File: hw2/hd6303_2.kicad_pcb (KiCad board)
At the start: 2 copper layers, 29 parts, among them J1 Conn_02x20_Odd_Even, J2 Conn_02x06_Odd_Even, J3 Screw_Terminal_01x02, SW1 SW_Push, U2 MAX708, U3 27C512, U4 HD6303RP, U5 HM62256BLP-7, U6 GAL16V8, Y1 4.9152M

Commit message: still making progress...
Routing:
- net /-WMEM: track 0.00 -> 74.9 mm, vias 0 -> 2
- net /-IOEN3: track 0.00 -> 71.3 mm, vias 0 -> 3
- net /-IOEN1: track 0.00 -> 71.0 mm, vias 0 -> 3
- net /-IOEN0: track 0.00 -> 70.9 mm, vias 0 -> 3
- net /-IOEN2: track 0.00 -> 69.7 mm, vias 0 -> 2
- net /A0: track 67.1 -> 135.7 mm, vias 2 -> 4
- net /A1: track 61.9 -> 125.8 mm, vias 2 -> 4
- net /A2: track 57.1 -> 115.8 mm, vias 0 -> 2
- net /A3: track 59.3 -> 111.6 mm, vias 2 -> 4
- net /A4: track 64.4 -> 112.0 mm, vias 2 -> 4
- net /A5: track 69.3 -> 112.8 mm, vias 2 -> 4
- net /A6: track 74.1 -> 113.0 mm, vias 2 -> 4
- net /A7: track 78.8 -> 110.9 mm, vias 1 -> 2
- net /P22: track 0.00 -> 23.2 mm, vias 0 -> 1
- net /P21: track 0.00 -> 22.5 mm, vias 0 -> 1
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
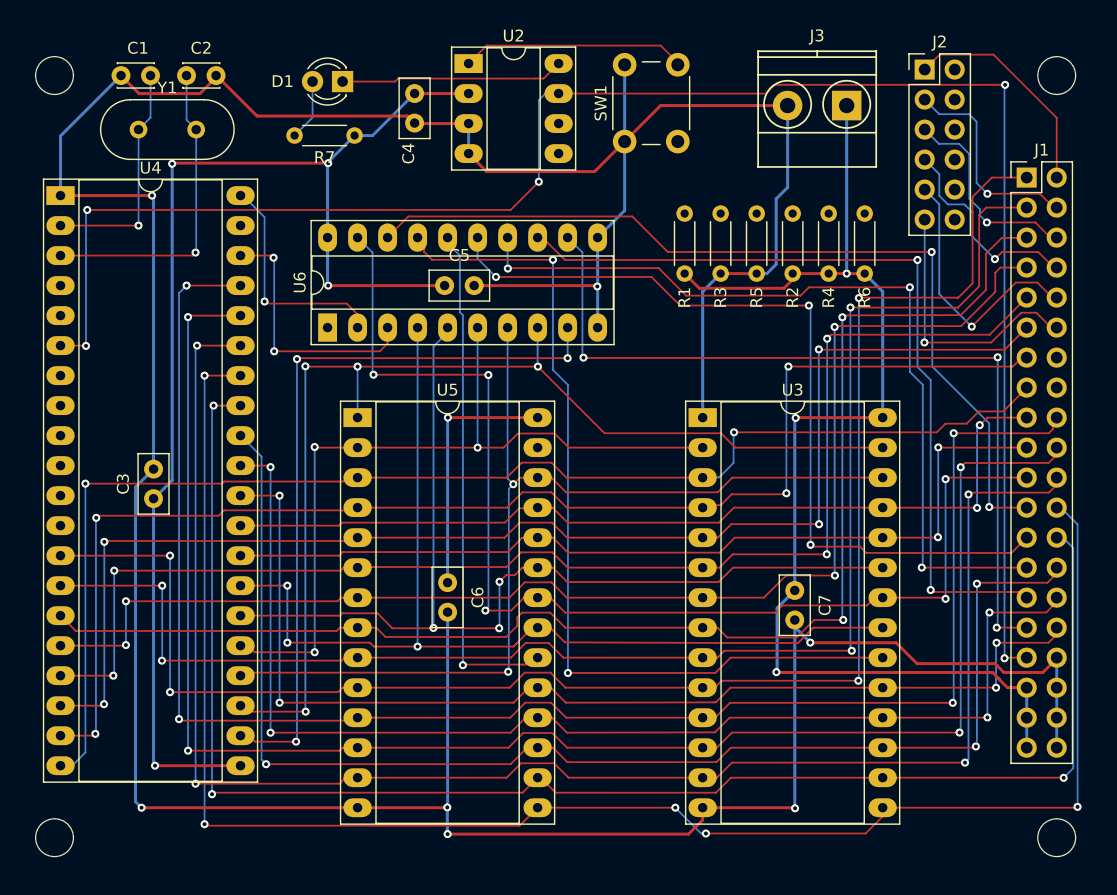
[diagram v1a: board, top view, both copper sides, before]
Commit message: all traces on expansion header routed
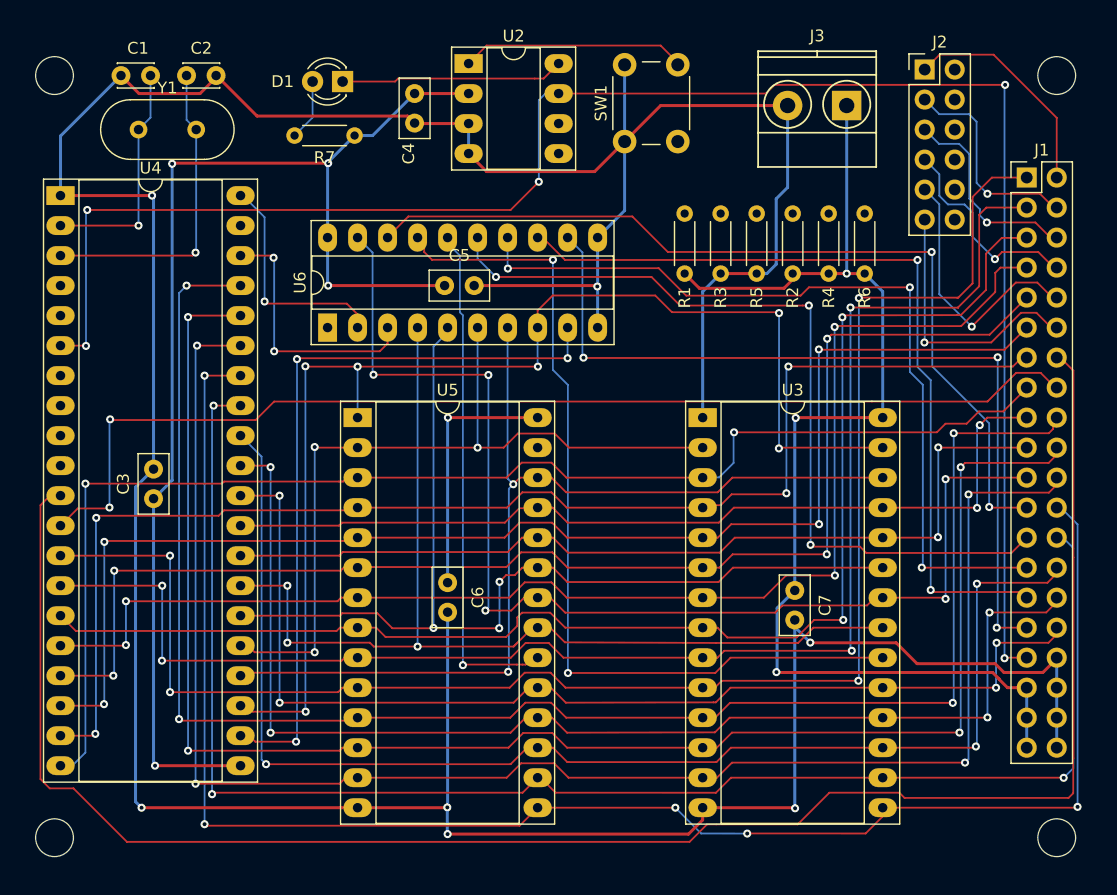
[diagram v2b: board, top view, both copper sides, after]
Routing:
- net /P23: track 0.00 -> 154.6 mm
- net /P24: track 0.00 -> 94.6 mm, vias 0 -> 2
- net /A14: track 94.4 -> 105.7 mm, vias 4 -> 6
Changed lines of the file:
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@@
   (general
     (links 155)
-    (no_connects 19)
+    (no_connects 17)
     (area 66.144857 85.645 178.203143 159.819)
     (thickness 1.6)
     (drawings 0)
-    (tracks 919)
+    (tracks 969)
     (zones 0)
     (modules 29)
@@
   (segment (start 83.058 146.304) (end 83.2104 146.1516) (width 0.1524) (layer F.Cu) (net 19))
   (segment (start 105.1814 127.2286) (end 105.41 127) (width 0.1524) (layer F.Cu) (net 19))
+  (segment (start 135.763 153.81224) (end 134.99084 153.81224) (width 0.1524) (layer F.Cu) (net 20))
+  (segment (start 142.66164 153.81224) (end 135.763 153.81224) (width 0.1524) (layer F.Cu) (net 20))
+  (segment (start 145.34388 151.13) (end 142.66164 153.81224) (width 0.1524) (layer F.Cu) (net 20))
+  (segment (start 151.26716 151.13) (end 145.34388 151.13) (width 0.1524) (layer F.Cu) (net 20))
+  (segment (start 151.70912 151.57196) (end 151.26716 151.13) (width 0.1524) (layer F.Cu) (net 20))
+  (segment (start 165.59276 151.57196) (end 151.70912 151.57196) (width 0.1524) (layer F.Cu) (net 20))
+  (segment (start 165.989 151.17572) (end 165.59276 151.57196) (width 0.1524) (layer F.Cu) (net 20))
+  (segment (start 165.989 148.2344) (end 165.989 151.17572) (width 0.1524) (layer F.Cu) (net 20))
+  (segment (start 166.00932 148.21408) (end 165.989 148.2344) (width 0.1524) (layer F.Cu) (net 20))
+  (segment (start 166.00932 131.21132) (end 166.00932 148.21408) (width 0.1524) (layer F.Cu) (net 20))
+  (segment (start 166.00424 131.20624) (end 166.00932 131.21132) (width 0.1524) (layer F.Cu) (net 20))
+  (segment (start 166.00424 127.635) (end 166.00424 131.20624) (width 0.1524) (layer F.Cu) (net 20))
+  (segment (start 166.00424 115.40744) (end 166.00424 127.635) (width 0.1524) (layer F.Cu) (net 20))
+  (segment (start 164.8968 114.3) (end 166.00424 115.40744) (width 0.1524) (layer F.Cu) (net 20) (status 400000))
+  (segment (start 78.56728 126.79172) (end 79.375 125.984) (width 0.1524) (layer F.Cu) (net 20) (status 800000))
+  (segment (start 78.56728 149.98192) (end 78.56728 126.79172) (width 0.1524) (layer F.Cu) (net 20))
+  (segment (start 79.3496 150.76424) (end 78.56728 149.98192) (width 0.1524) (layer F.Cu) (net 20))
+  (segment (start 81.36128 150.76424) (end 79.3496 150.76424) (width 0.1524) (layer F.Cu) (net 20))
+  (segment (start 85.88756 155.29052) (end 81.36128 150.76424) (width 0.1524) (layer F.Cu) (net 20))
+  (segment (start 133.51256 155.29052) (end 85.88756 155.29052) (width 0.1524) (layer F.Cu) (net 20))
+  (segment (start 134.99084 153.81224) (end 133.51256 155.29052) (width 0.1524) (layer F.Cu) (net 20))
+  (segment (start 79.375 125.984) (end 80.264 125.984) (width 0.1524) (layer F.Cu) (net 20) (status C00000))
+  (segment (start 164.592 114.3) (end 164.8968 114.3) (width 0.1524) (layer F.Cu) (net 20) (status C00000))
   (segment (start 162.052 116.84) (end 162.052 116.87556) (width 0.1524) (layer F.Cu) (net 21) (status C00000))
   (segment (start 162.052 116.87556) (end 160.0708 118.85676) (width 0.1524) (layer F.Cu) (net 21) (status 400000))
@@
   (segment (start 104.1908 124.7902) (end 104.521 124.46) (width 0.1524) (layer F.Cu) (net 21))
   (segment (start 104.521 124.46) (end 105.41 124.46) (width 0.1524) (layer F.Cu) (net 21))
+  (segment (start 148.95068 118.01856) (end 98.3488 118.01856) (width 0.1524) (layer F.Cu) (net 22))
+  (segment (start 158.72968 118.01856) (end 148.95068 118.01856) (width 0.1524) (layer F.Cu) (net 22))
+  (segment (start 161.15792 115.59032) (end 158.72968 118.01856) (width 0.1524) (layer F.Cu) (net 22))
+  (segment (start 163.23056 115.59032) (end 161.15792 115.59032) (width 0.1524) (layer F.Cu) (net 22))
+  (segment (start 164.48024 116.84) (end 163.23056 115.59032) (width 0.1524) (layer F.Cu) (net 22) (status 400000))
+  (segment (start 81.71688 127.07112) (end 80.264 128.524) (width 0.1524) (layer F.Cu) (net 22) (status 800000))
+  (segment (start 84.328 127.07112) (end 81.71688 127.07112) (width 0.1524) (layer F.Cu) (net 22))
+  (segment (start 84.40928 126.98984) (end 84.328 127.07112) (width 0.1524) (layer F.Cu) (net 22))
+  (via (at 84.40928 126.98984) (size 0.6858) (drill 0.3302) (layers F.Cu B.Cu) (net 22))
+  (segment (start 84.40928 119.5832) (end 84.40928 126.98984) (width 0.1524) (layer B.Cu) (net 22))
+  (segment (start 84.46516 119.52732) (end 84.40928 119.5832) (width 0.1524) (layer B.Cu) (net 22))
+  (via (at 84.46516 119.52732) (size 0.6858) (drill 0.3302) (layers F.Cu B.Cu) (net 22))
+  (segment (start 84.52104 119.5832) (end 84.46516 119.52732) (width 0.1524) (layer F.Cu) (net 22))
+  (segment (start 96.78416 119.5832) (end 84.52104 119.5832) (width 0.1524) (layer F.Cu) (net 22))
+  (segment (start 98.3488 118.01856) (end 96.78416 119.5832) (width 0.1524) (layer F.Cu) (net 22))
+  (segment (start 164.592 116.84) (end 164.48024 116.84) (width 0.1524) (layer F.Cu) (net 22) (status C00000))
   (segment (start 162.052 119.38) (end 158.71444 119.38) (width 0.1524) (layer F.Cu) (net 23) (status 400000))
   (segment (start 157.82544 127) (end 149.86 127) (width 0.1524) (layer F.Cu) (net 23) (status 800000))
@@
   (segment (start 158.877 126.9492) (end 158.9278 127) (width 0.1524) (layer F.Cu) (net 29))
   (segment (start 158.9278 127) (end 162.052 127) (width 0.1524) (layer F.Cu) (net 29) (status 800000))
+  (via (at 138.39444 154.58948) (size 0.6858) (drill 0.3302) (layers F.Cu B.Cu) (net 30))
+  (via (at 132.3086 152.4) (size 0.6858) (drill 0.3302) (layers F.Cu B.Cu) (net 30))
+  (segment (start 132.3086 152.4) (end 134.493 154.5844) (width 0.1524) (layer B.Cu) (net 30))
+  (segment (start 134.493 154.5844) (end 138.39444 154.58948) (width 0.1524) (layer B.Cu) (net 30))
+  (segment (start 120.65 152.4) (end 132.3086 152.4) (width 0.1524) (layer F.Cu) (net 30))
+  (segment (start 138.394445 154.589475) (end 138.394445 154.57932) (width 0.1524) (layer F.Cu) (net 30))
+  (segment (start 138.39444 154.58948) (end 138.394445 154.589475) (width 0.1524) (layer F.Cu) (net 30))
   (segment (start 164.592 127) (end 164.94252 127) (width 0.1524) (layer B.Cu) (net 30))
   (segment (start 164.94252 127) (end 166.35476 128.41224) (width 0.1524) (layer B.Cu) (net 30))
@@
   (segment (start 166.35476 152.32888) (end 166.28364 152.4) (width 0.1524) (layer F.Cu) (net 30))
   (segment (start 166.28364 152.4) (end 149.86 152.4) (width 0.1524) (layer F.Cu) (net 30))
-  (segment (start 120.65 152.4) (end 132.3086 152.4) (width 0.1524) (layer F.Cu) (net 30))
   (segment (start 148.4122 154.5844) (end 149.86 153.1366) (width 0.1524) (layer F.Cu) (net 30))
-  (segment (start 134.8994 154.5844) (end 148.4122 154.5844) (width 0.1524) (layer F.Cu) (net 30))
-  (via (at 134.8994 154.5844) (size 0.6858) (drill 0.3302) (layers F.Cu B.Cu) (net 30))
-  (segment (start 134.493 154.5844) (end 134.8994 154.5844) (width 0.1524) (layer B.Cu) (net 30))
-  (segment (start 132.3086 152.4) (end 134.493 154.5844) (width 0.1524) (layer B.Cu) (net 30))
-  (via (at 132.3086 152.4) (size 0.6858) (drill 0.3302) (layers F.Cu B.Cu) (net 30))
+  (segment (start 138.394445 154.57932) (end 148.4122 154.5844) (width 0.1524) (layer F.Cu) (net 30))
+  (segment (start 138.39444 154.57932) (end 138.394445 154.57932) (width 0.1524) (layer F.Cu) (net 30))
   (segment (start 149.86 153.1366) (end 149.86 152.4) (width 0.1524) (layer F.Cu) (net 30))
   (segment (start 95.504 115.824) (end 92.456 115.824) (width 0.1524) (layer F.Cu) (net 30))
@@
   (segment (start 119.1514 124.46) (end 118.5926 125.0188) (width 0.1524) (layer F.Cu) (net 52))
   (segment (start 95.758 140.97) (end 95.504 141.224) (width 0.1524) (layer F.Cu) (net 52))
-  (segment (start 149.86 121.92) (end 137.3886 121.92) (width 0.1524) (layer F.Cu) (net 53))
-  (segment (start 126.3142 120.7008) (end 120.6754 115.062) (width 0.1524) (layer F.Cu) (net 53))
-  (segment (start 136.1694 120.7008) (end 126.3142 120.7008) (width 0.1524) (layer F.Cu) (net 53))
-  (segment (start 137.3886 121.92) (end 136.1694 120.7008) (width 0.1524) (layer F.Cu) (net 53))
+  (segment (start 149.86 121.92) (end 141.13764 121.92) (width 0.1524) (layer F.Cu) (net 53) (status 400000))
+  (segment (start 120.65 110.31728) (end 120.65 111.76) (width 0.1524) (layer F.Cu) (net 53) (status 800000))
+  (segment (start 121.92508 109.0422) (end 120.65 110.31728) (width 0.1524) (layer F.Cu) (net 53))
+  (segment (start 130.6068 109.0422) (end 121.92508 109.0422) (width 0.1524) (layer F.Cu) (net 53))
+  (segment (start 132.01904 110.45444) (end 130.6068 109.0422) (width 0.1524) (layer F.Cu) (net 53))
+  (segment (start 141.01064 110.45444) (end 132.01904 110.45444) (width 0.1524) (layer F.Cu) (net 53))
+  (segment (start 141.08684 110.53064) (end 141.01064 110.45444) (width 0.1524) (layer F.Cu) (net 53))
+  (via (at 141.08684 110.53064) (size 0.6858) (drill 0.3302) (layers F.Cu B.Cu) (net 53))
+  (segment (start 141.08684 121.9708) (end 141.08684 110.53064) (width 0.1524) (layer B.Cu) (net 53))
+  (segment (start 141.0716 121.98604) (end 141.08684 121.9708) (width 0.1524) (layer B.Cu) (net 53))
+  (via (at 141.0716 121.98604) (size 0.6858) (drill 0.3302) (layers F.Cu B.Cu) (net 53))
+  (segment (start 141.13764 121.92) (end 141.0716 121.98604) (width 0.1524) (layer F.Cu) (net 53))
   (segment (start 105.41 119.38) (end 105.41 115.062) (width 0.1524) (layer B.Cu) (net 53))
   (segment (start 105.41 115.062) (end 105.4354 115.062) (width 0.1524) (layer F.Cu) (net 53))
